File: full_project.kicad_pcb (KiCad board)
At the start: 2 copper layers, 57.4 x 85.9 mm, 34 parts, among them J1 Conn_01x02, J10 V2(pH), J11 Conn_01x02, J12 V_OFFSET, J13 AltpH_V(pH), J14 Conn_01x02, J2 Raspberry_Pi_2_3, J3 Conn_01x05_Titrator, J4 Screw_Terminal_01x04_titrator, J5 RF_Shield_Two_Pieces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

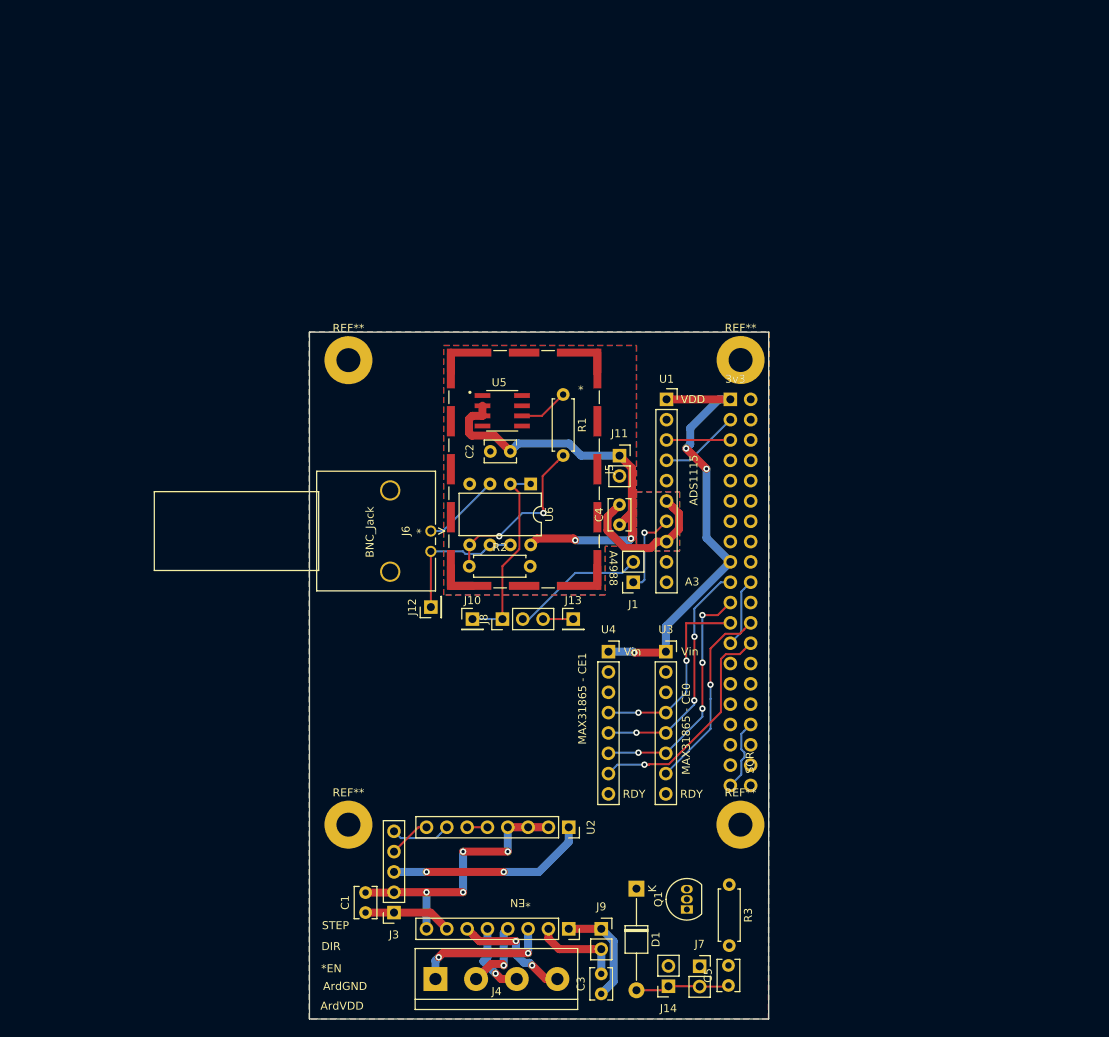
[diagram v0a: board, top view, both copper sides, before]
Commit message: Used git like a big boy
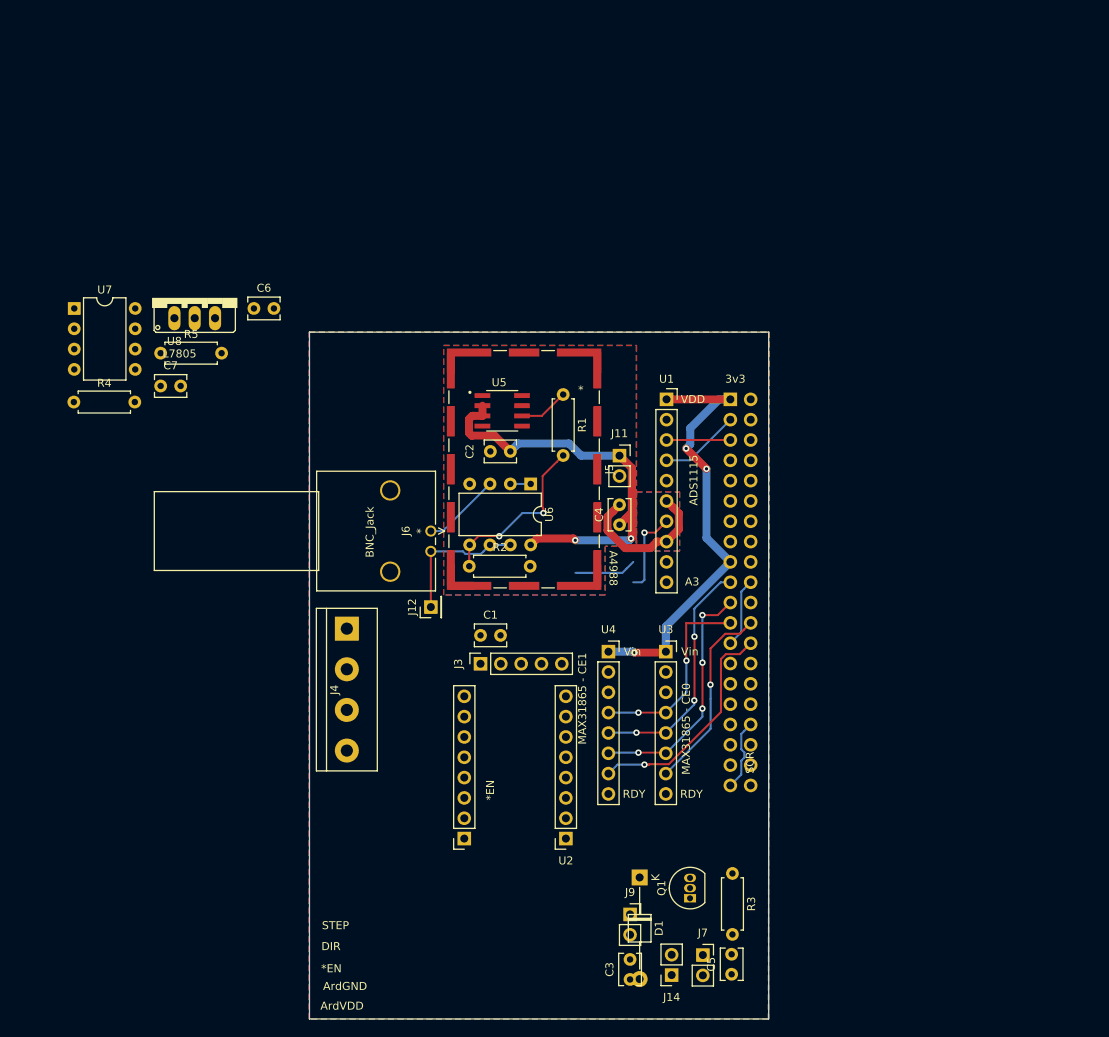
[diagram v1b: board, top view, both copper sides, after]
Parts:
- removed J1: Conn_01x02, Connector_PinSocket_2.54mm:PinSocket_1x02_P2.54mm_Vertical
- removed J10: V2(pH), Connector_PinHeader_2.54mm:PinHeader_1x01_P2.54mm_Vertical
- removed J13: AltpH_V(pH), Connector_PinHeader_2.54mm:PinHeader_1x01_P2.54mm_Vertical
- removed J8: Conn_01x03, Connector_PinHeader_2.54mm:PinHeader_1x03_P2.54mm_Vertical
- removed REF** (x4): MountingHole_3mm_Pad, MountingHole:MountingHole_3mm_Pad
- added C6: 1uF, Capacitor_THT:C_Disc_D3.8mm_W2.6mm_P2.50mm, F.Cu at (120.7, 53.7)
- added C7: 1uF, Capacitor_THT:C_Disc_D3.8mm_W2.6mm_P2.50mm, F.Cu at (109.0, 63.4)
- added R4: 160000, Resistor_THT:R_Axial_DIN0207_L6.3mm_D2.5mm_P7.62mm_Horizontal, F.Cu at (98.2, 65.4)
- added R5: 160000, Resistor_THT:R_Axial_DIN0207_L6.3mm_D2.5mm_P7.62mm_Horizontal, F.Cu at (109.0, 59.3)
- added U7: LMC662, Package_DIP:DIP-8_W7.62mm, F.Cu at (98.2, 53.7)
- added U8: L7805, L7805:78XXS, F.Cu at (113.3, 52.4)
- moved J4 45.2 mm to (132.3, 93.7), turned to 270 degrees
- moved C1 37.5 mm to (149.0, 94.5), turned to 0 degrees
- moved J3 32.9 mm to (149.0, 98.1), turned to 90 degrees
- moved J9 4.02 mm to (167.7, 129.4)
- moved C3 4.02 mm to (167.7, 137.6)
- moved U2 1.46 mm to (159.7, 119.9), turned to 180 degrees
- moved C5 1.46 mm to (180.4, 136.9)
- moved D1 1.46 mm to (168.9, 124.8)
- moved J14 1.46 mm to (172.9, 137.0)
- moved J7 1.46 mm to (176.8, 134.5)
- moved R3 1.46 mm to (180.5, 124.3)
- moved Q1 1.46 mm to (175.2, 127.4)
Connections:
- U1 pad 1: +3V3 -> +5V
- U1 pad 7: Net-(J1-Pad1) -> /PSU_5VGND
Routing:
- net /Arduino_GND: track 35.6 -> 0.00 mm, vias 4 -> 0
- net /*EN: track 25.2 -> 0.00 mm, vias 2 -> 0
- net Net-(R5-Pad2): track 24.5 -> 2.54 mm
- net Net-(J4-Pad1): track 17.3 -> 0.00 mm, vias 2 -> 0
- net Net-(J4-Pad4): track 14.9 -> 0.00 mm, vias 2 -> 0
- net /PSU_12V: track 13.5 -> 0.00 mm
- net /PSU_12VGND: track 11.4 -> 0.00 mm
- net Net-(C5-Pad1): track 11.4 -> 0.00 mm
- net /Arduino_VDD: track 11.0 -> 0.00 mm
- net Net-(J1-Pad1): track 10.8 -> 0.00 mm, vias 1 -> 0
- net /PSU_5VGND: track 31.6 -> 42.3 mm, vias 0 -> 1
- net Net-(J4-Pad3): track 9.36 -> 0.00 mm, vias 1 -> 0
- net Net-(J4-Pad2): track 9.09 -> 0.00 mm, vias 1 -> 0
- net Net-(J1-Pad2): track 16.8 -> 7.80 mm
- net /STEP: track 7.52 -> 0.00 mm
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
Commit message: Added LCD and Keypad connectors, switched PSU connector to screw terminal, updated footprints, and added datasheets to parts.
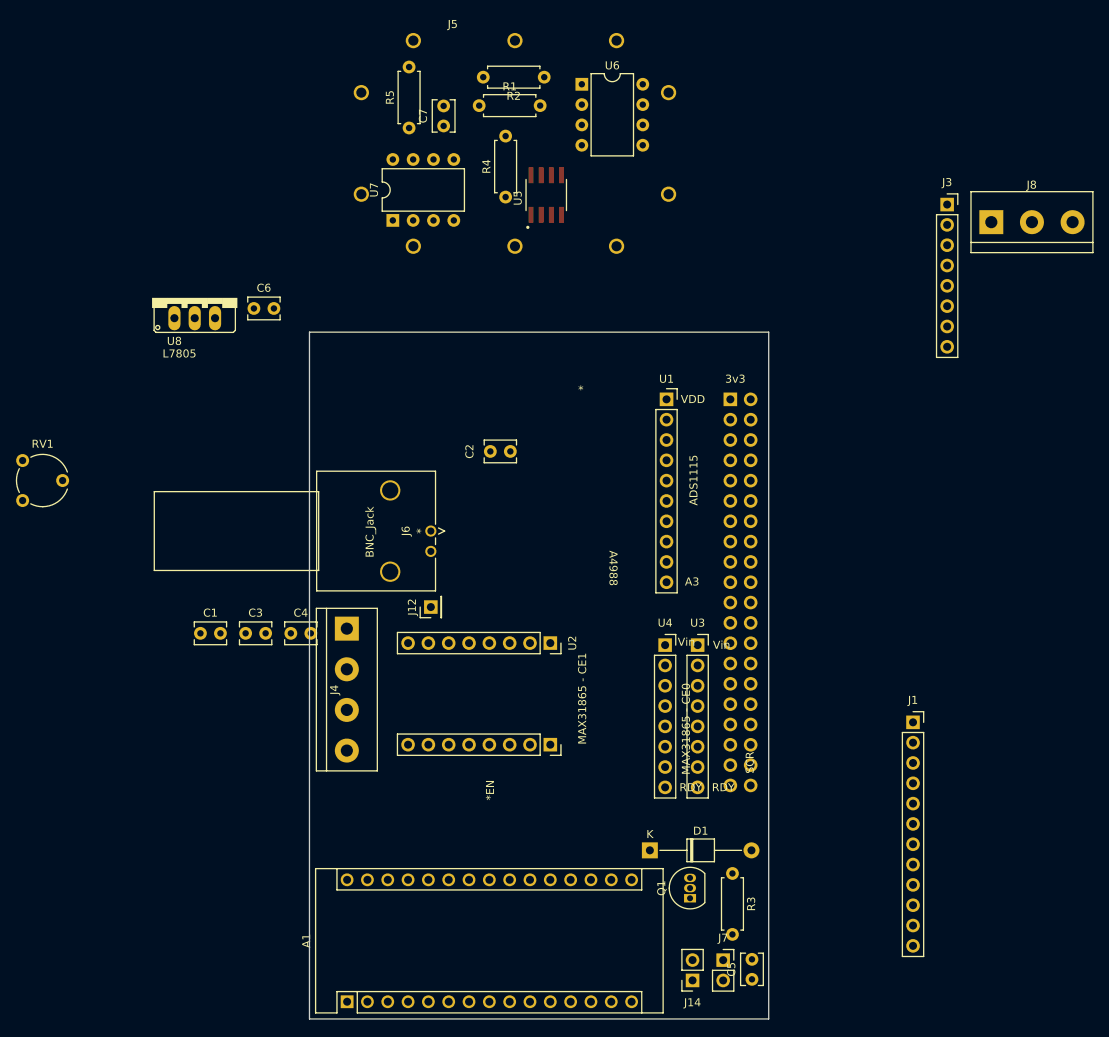
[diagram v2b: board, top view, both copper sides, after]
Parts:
- removed J11, J9: Conn_01x02, Connector_PinSocket_2.54mm:PinSocket_1x02_P2.54mm_Vertical
- added A1: Arduino_Nano_v3.x, Module:Arduino_Nano, F.Cu at (132.3, 140.3)
- added J1: Conn_01x12, Connector_PinSocket_2.54mm:PinSocket_1x12_P2.54mm_Vertical, F.Cu at (203.1, 105.4)
- added J8: Screw_Terminal_01x03, TerminalBlock:TerminalBlock_bornier-3_P5.08mm, F.Cu at (212.9, 42.9)
- added RV1: R_POT, Potentiometer_THT:Potentiometer_Piher_PT-6-V_Vertical, F.Cu at (91.8, 77.7)
- C1: value .1uF -> 0.1uF
- C4: value 0.1uF -> .1uF
- J3: value Conn_01x05_Titrator -> Conn_01x08; footprint Connector_PinSocket_2.54mm:PinSocket_1x05_P2.54mm_Vertical -> Connector_PinSocket_2.54mm:PinSocket_1x08_P2.54mm_Vertical
- J5: footprint RF_Shielding:Laird_Technologies_BMI-S-209-F_29.36x18.50mm -> Titrator_Footprints:44-CBSA-1.0X1.5X0.4
- U8: footprint L7805:78XXS -> Titrator_Footprints:78XXS
- moved J3 81.8 mm to (207.3, 40.7), turned to 0 degrees
- moved C3 64.7 mm to (119.6, 94.3), turned to 0 degrees
- moved R2 61.8 mm to (157.0, 24.8), turned to 180 degrees
- moved R4 59.7 mm to (152.1, 39.8), turned to 90 degrees
- moved J5 57.3 mm to (134.1, 20.2), turned to 0 degrees
- moved U6 50.4 mm to (161.7, 25.7), turned to 0 degrees
- moved C7 48.0 mm to (144.4, 30.9), turned to 90 degrees
- moved C4 43.3 mm to (125.3, 94.3), turned to 0 degrees
- moved R5 41.9 mm to (140.1, 31.1), turned to 90 degrees
- moved U7 41.3 mm to (138.0, 42.7), turned to 90 degrees
- moved R1 37.6 mm to (148.8, 28.3), turned to 0 degrees
- moved C1 35.0 mm to (114.0, 94.3)
- moved U5 27.5 mm to (157.2, 39.5), turned to 90 degrees
- moved U2 24.5 mm to (157.7, 95.5), turned to 270 degrees
- moved U4 7.13 mm to (172.1, 95.8)
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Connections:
- C1 pad 1: /Arduino_VDD -> /PSU_5V
- C1 pad 2: /Arduino_GND -> /PSU_GND
- C2 pad 1: /PSU_5V -> /PSU_A5V
- C2 pad 2: /PSU_5VGND -> /PSU_AGND
- C3 pad 2: /PSU_12VGND -> /PSU_GND
- C4 pad 1: /PSU_5V -> /Arduino_VDD
- C4 pad 2: /PSU_5VGND -> /Arduino_GND
- C6 pad 1: /PSU_5VGND -> /PSU_AGND
- C7 pad 2: /PSU_5VGND -> /PSU_AGND
- J2 pad 10: Net-(J2-Pad10) -> (no net)
- J2 pad 11: Net-(J2-Pad11) -> (no net)
- J2 pad 12: Net-(J2-Pad12) -> /LCD_D7
- J2 pad 13: Net-(J2-Pad13) -> /LCD_RS
- J2 pad 15: Net-(J2-Pad15) -> /LCD_E
- J2 pad 16: Net-(J2-Pad16) -> /LCD_D6
- J2 pad 18: Net-(J2-Pad18) -> /LCD_D5
- J2 pad 2: Net-(J2-Pad2) -> /PSU_5V
- J2 pad 22: Net-(J2-Pad22) -> /LCD_D4
- J2 pad 27: Net-(J2-Pad27) -> (no net)
- J2 pad 28: Net-(J2-Pad28) -> /KeyCol_1
- J2 pad 29: Net-(J2-Pad29) -> (no net)
- J2 pad 31: Net-(J2-Pad31) -> /KeyRow_1
- J2 pad 33: Net-(J2-Pad33) -> /KeyRow_2
- J2 pad 35: Net-(J2-Pad35) -> /KeyRow_3
- J2 pad 36: Net-(J2-Pad36) -> /KeyCol_2
- J2 pad 37: Net-(J2-Pad37) -> /KeyRow_4
- J2 pad 38: Net-(J2-Pad38) -> /KeyCol_3
- J2 pad 4: Net-(J2-Pad4) -> +5V
- J2 pad 40: Net-(J2-Pad40) -> /KeyCol_4
- J2 pad 6: GND -> /PSU_GND
- J2 pad 7: Net-(J2-Pad7) -> (no net)
- J2 pad 8: Net-(J2-Pad8) -> (no net)
- J3 pad 1: /Arduino_VDD -> /KeyRow_1
- J3 pad 2: /Arduino_GND -> /KeyRow_2
- J3 pad 3: /*EN -> /KeyRow_3
- J3 pad 4: /DIR -> /KeyRow_4
- J3 pad 5: /STEP -> /KeyCol_1
- J5 pad 1: /PSU_5VGND -> /PSU_AGND
- J6 pad 3: Net-(J6-Pad3) -> (no net)
- J6 pad 4: Net-(J6-Pad4) -> (no net)
- R2 pad 2: /PSU_5VGND -> /PSU_AGND
- U1 pad 10: Net-(U1-Pad10) -> (no net)
- U1 pad 6: /PSU_5VGND -> /PSU_AGND
- U1 pad 7: /PSU_5VGND -> /PSU_AGND
- U1 pad 8: /PSU_5VGND -> /PSU_AGND
- U1 pad 9: Net-(U1-Pad9) -> (no net)
- U2 pad 1: /*EN -> /Arduino_GND
- U2 pad 10: /PSU_12VGND -> /PSU_GND
- U3 pad 3: Net-(U3-Pad3) -> (no net)
- U3 pad 8: Net-(U3-Pad8) -> (no net)
- U4 pad 3: Net-(U4-Pad3) -> (no net)
- U4 pad 8: Net-(U4-Pad8) -> (no net)
- U5 pad 1: /PSU_5VGND -> /PSU_AGND
- U5 pad 2: /PSU_5V -> /PSU_A5V
- U5 pad 3: /PSU_5V -> /PSU_A5V
- U5 pad 4: /PSU_5VGND -> /PSU_AGND
- U5 pad 5: Net-(U5-Pad5) -> (no net)
- U5 pad 7: /PSU_5VGND -> /PSU_AGND
- U5 pad 8: /PSU_5VGND -> /PSU_AGND
- U6 pad 4: /PSU_5VGND -> /PSU_AGND
- U6 pad 8: /PSU_5V -> /PSU_A5V
- U7 pad 1: /PSU_5VGND -> /PSU_AGND
- U7 pad 2: /PSU_5VGND -> /PSU_AGND
- U7 pad 4: /PSU_5VGND -> /PSU_AGND
- U7 pad 5: Net-(U7-Pad5) -> (no net)
- U7 pad 6: Net-(U7-Pad6) -> (no net)
- U7 pad 7: Net-(U7-Pad7) -> (no net)
- U7 pad 8: /PSU_5V -> /PSU_A5V
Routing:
- net /PSU_5V: track 57.5 -> 0.00 mm, vias 2 -> 0
- net +3V3: track 55.5 -> 0.00 mm, vias 3 -> 0
- net /PSU_5VGND: track 42.3 -> 0.00 mm, vias 1 -> 0
- net /MISO: track 30.7 -> 0.00 mm, vias 4 -> 0
- net /MOSI: track 30.3 -> 0.00 mm, vias 3 -> 0
- net /CE1: track 28.4 -> 0.00 mm, vias 1 -> 0
- net /SCLK: track 25.0 -> 0.00 mm, vias 2 -> 0
- net /CE0: track 24.3 -> 0.00 mm, vias 1 -> 0
- net Net-(R1-Pad2): track 21.9 -> 0.00 mm, vias 2 -> 0
- net GND: track 17.7 -> 0.00 mm
- net Net-(J12-Pad1): track 17.5 -> 0.00 mm
- net /SDA: track 10.1 -> 0.00 mm
- net Net-(J6-Pad1): track 9.84 -> 0.00 mm
- net /SCL: track 7.98 -> 0.00 mm
- net Net-(J1-Pad2): track 7.80 -> 0.00 mm
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- removed copper zone on B.Cu, net /PSU_5VGND
- removed copper zone on F.Cu, net /PSU_5VGND
- removed copper zone on B.Cu, net GND
- removed copper zone on F.Cu, net GND
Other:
- board text removed: "ArdGND"
- board text removed: "ArdVDD"
- board text removed: "DIR"
- board text removed: "STEP"

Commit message: layed out PCB
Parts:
- added REF**: MountingHole_3mm_Pad, MountingHole:MountingHole_3mm_Pad, F.Cu at (132.5, 118.2)
- added REF**: MountingHole_3mm_Pad, MountingHole:MountingHole_3mm_Pad, F.Cu at (181.5, 118.2)
- added REF**: MountingHole_3mm_Pad, MountingHole:MountingHole_3mm_Pad, F.Cu at (181.5, 60.1)
- added REF**: MountingHole_3mm_Pad, MountingHole:MountingHole_3mm_Pad, F.Cu at (132.5, 60.1)
- moved J8 99.3 mm to (183.8, 137.8), turned to 90 degrees
- moved RV1 78.0 mm to (168.3, 63.0)
- moved J5 77.4 mm to (138.7, 97.5), turned to 90 degrees
- moved C1 70.4 mm to (176.6, 62.0), turned to 270 degrees
- moved C3 68.5 mm to (177.9, 130.2), turned to 90 degrees
- moved J3 63.2 mm to (176.6, 95.8)
- moved U6 56.8 mm to (148.9, 81.0), turned to 180 degrees
- moved C7 48.2 mm to (161.6, 75.9), turned to 270 degrees
- moved R2 47.2 mm to (144.4, 70.2), turned to 0 degrees
- moved J1 43.7 mm to (186.5, 65.0)
- moved U7 43.6 mm to (158.8, 81.0), turned to 180 degrees
- moved A1 41.2 mm to (170.6, 125.1), turned to 270 degrees
- moved U8 39.7 mm to (132.7, 87.0), turned to 270 degrees
- moved C6 38.0 mm to (156.4, 66.5)
- moved R5 37.7 mm to (159.7, 63.3), turned to 180 degrees
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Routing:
- net GND: track 0.00 -> 173.1 mm, vias 0 -> 3
- net /PSU_GND: track 0.00 -> 155.4 mm, vias 0 -> 10
- net /PSU_12V: track 0.00 -> 100.6 mm, vias 0 -> 4
- net /PSU_5V: track 0.00 -> 82.5 mm
- net /Arduino_GND: track 0.00 -> 81.3 mm, vias 0 -> 3
- net +3V3: track 0.00 -> 50.4 mm, vias 0 -> 1
- net /PSU_A5V: track 0.00 -> 50.4 mm, vias 0 -> 1
- net /PWM: track 0.00 -> 44.2 mm, vias 0 -> 2
- net /DIR: track 0.00 -> 41.4 mm, vias 0 -> 1
- net Net-(J4-Pad1): track 0.00 -> 39.0 mm, vias 0 -> 3
- net /Arduino_VDD: track 0.00 -> 36.7 mm
- net Net-(C5-Pad1): track 0.00 -> 34.6 mm
- net Net-(J4-Pad2): track 0.00 -> 34.3 mm, vias 0 -> 3
- net /CE0: track 0.00 -> 32.5 mm, vias 0 -> 2
- net /CE1: track 0.00 -> 31.4 mm, vias 0 -> 1
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- added copper zone on B.Cu, net /PSU_AGND
- added copper zone on F.Cu, net /PSU_AGND
- added copper zone on B.Cu, net GND
- added copper zone on F.Cu, net GND
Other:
- board size 57.4 x 85.9 mm -> 61.4 x 85.9 mm

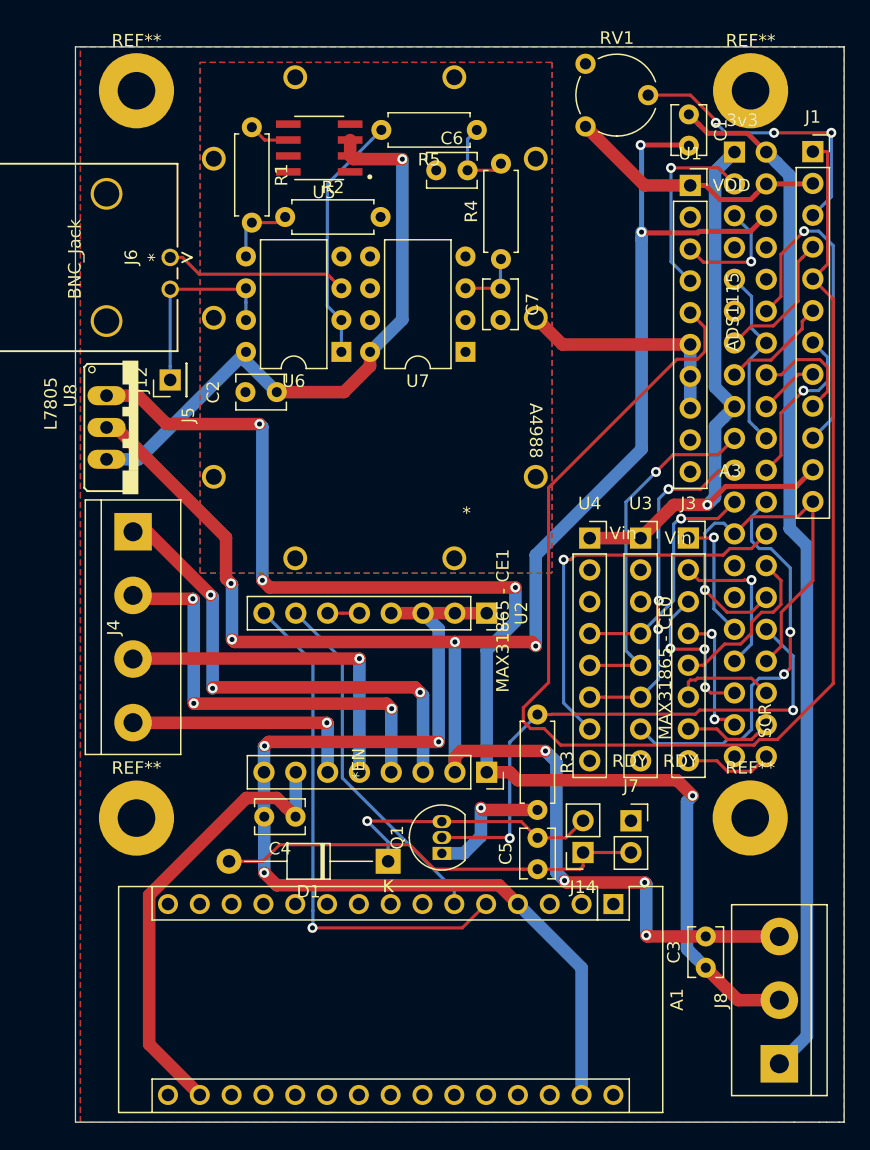
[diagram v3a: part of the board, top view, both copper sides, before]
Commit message: fixed screw terminal placement and ground plane overlaps
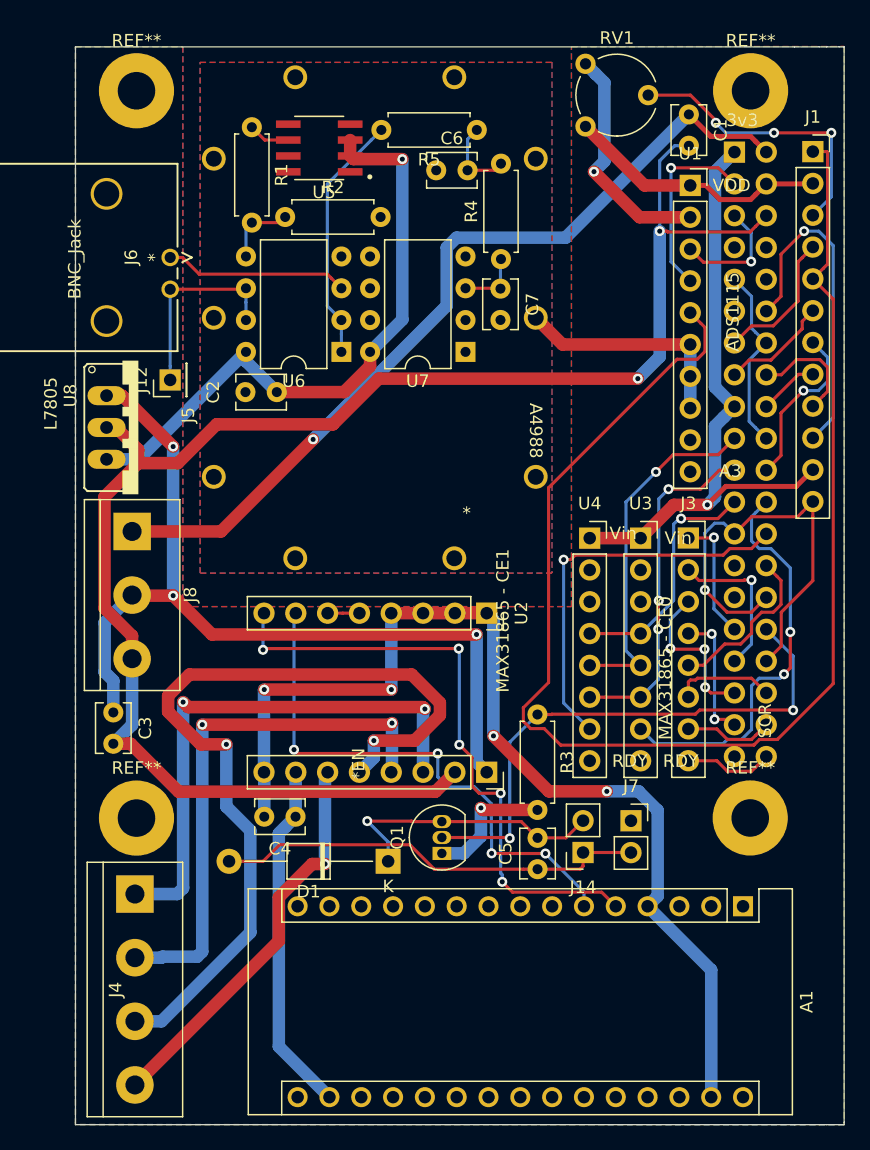
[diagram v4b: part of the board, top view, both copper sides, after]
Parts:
- moved J8 66.9 mm to (132.2, 95.3), turned to 270 degrees
- moved C3 51.5 mm to (130.7, 109.8), turned to 270 degrees
- moved J4 28.9 mm to (132.4, 124.3)
- moved A1 10.4 mm to (180.9, 125.2)
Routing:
- net Net-(J4-Pad3): track 27.2 -> 68.4 mm, vias 1 -> 2
- net /PSU_12V: track 100.6 -> 69.6 mm, vias 4 -> 3
- net /PSU_GND: track 155.4 -> 131.6 mm, vias 10 -> 2
- net GND: track 173.1 -> 191.9 mm, vias 3 -> 4
- net /STEP: track 28.5 -> 43.4 mm, vias 0 -> 4
- net /PSU_5V: track 82.5 -> 68.4 mm, vias 0 -> 1
- net Net-(J4-Pad4): track 19.5 -> 31.9 mm
- net /Arduino_VDD: track 36.7 -> 28.2 mm
- net Net-(J4-Pad2): track 34.3 -> 42.9 mm, vias 3 -> 2
- net /DIR: track 41.4 -> 49.6 mm, vias 1 -> 5
- net Net-(J4-Pad1): track 39.0 -> 43.5 mm, vias 3 -> 2
- net /Arduino_GND: track 81.3 -> 85.0 mm, vias 3 -> 4
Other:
- board size 61.4 x 85.9 mm -> 61.4 x 86.1 mm
